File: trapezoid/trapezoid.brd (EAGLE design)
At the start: 90 x 35 mm, 30 parts, among them IC2 LGD20H, U1 MMA8452Q, U2 microSD, U4 MCP73831, Y1 CRYSTAL.ABS25

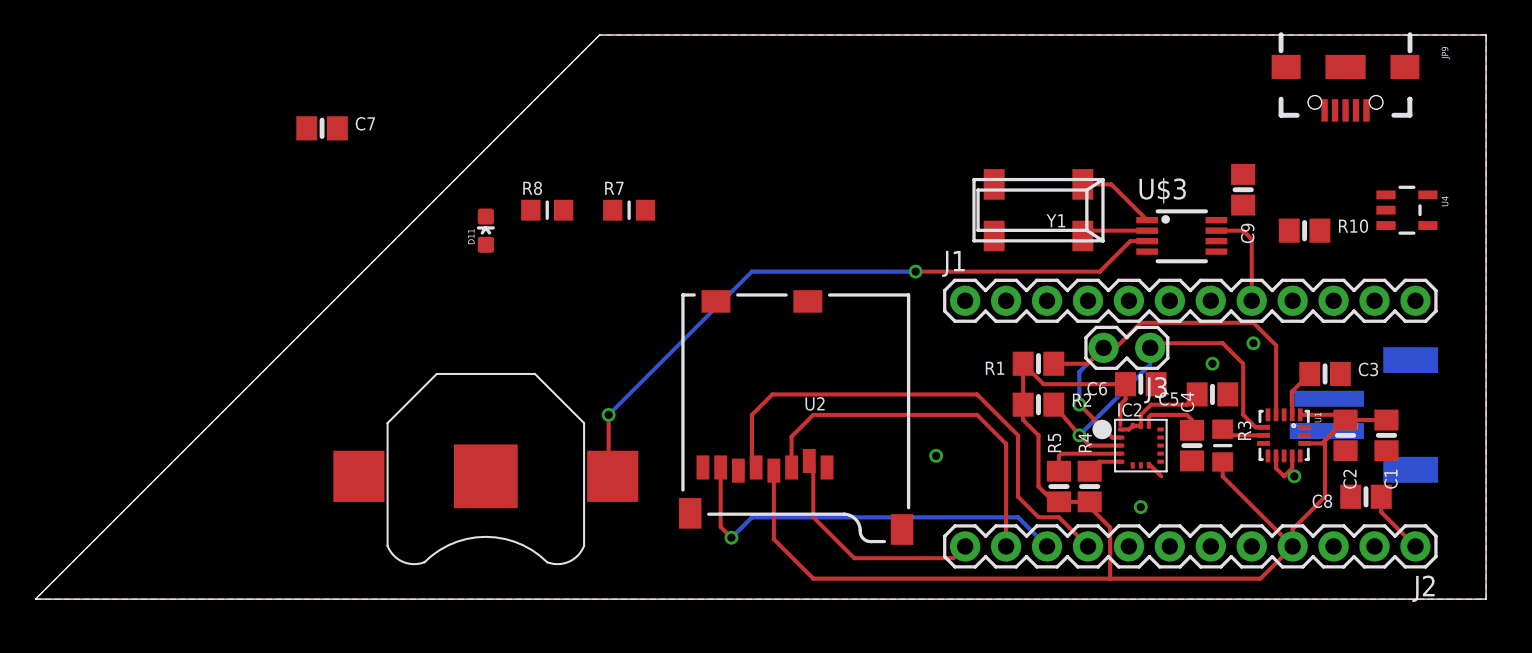
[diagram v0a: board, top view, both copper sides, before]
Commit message: fully connected schematics
had to remove some header pin spots to run wire
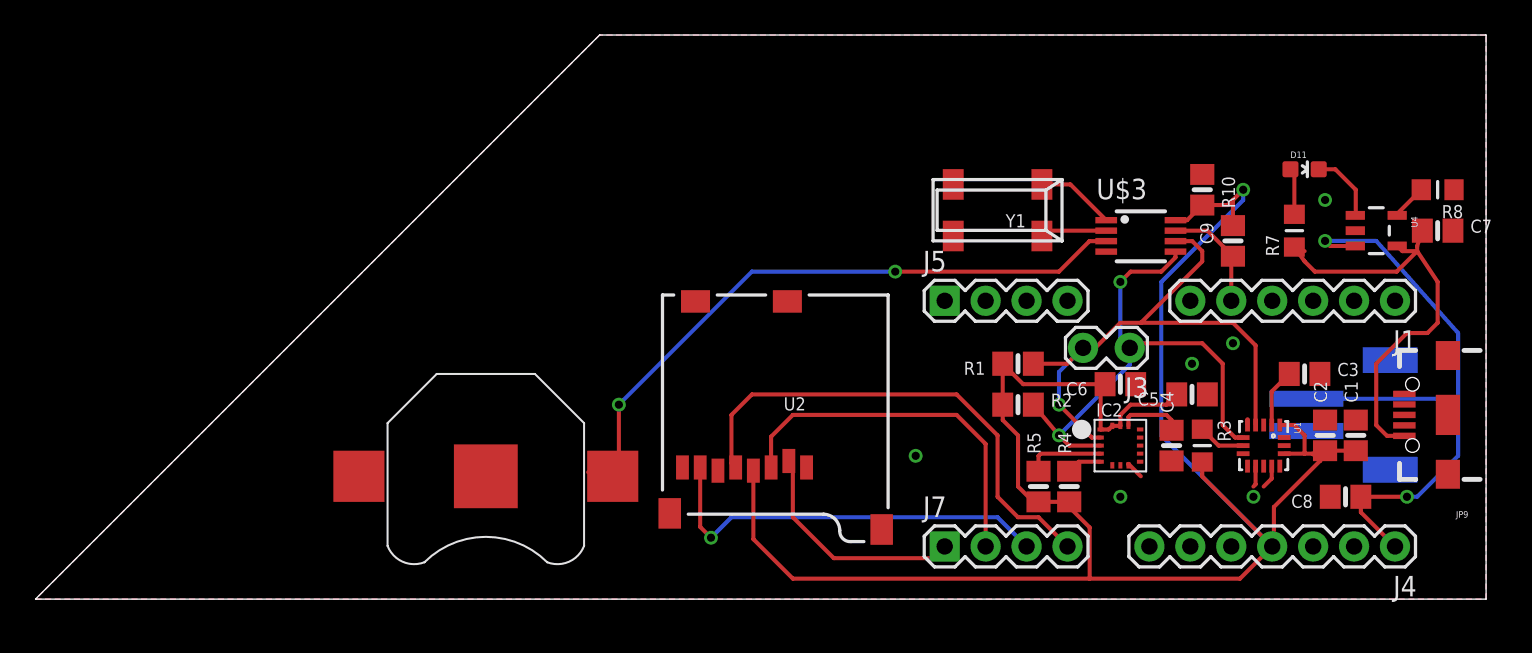
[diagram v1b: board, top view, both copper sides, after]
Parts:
- removed J2: (no value), SparkFun-Connectors:1X12
- added J4: (no value), SparkFun-Connectors:1X07
- added J5, J7: (no value), SparkFun-Connectors:1X04
- J1: device SparkFun-Connectors:1X12 -> SparkFun-Connectors:1X06
- moved C7 69.5 mm to (87.0, 22.9)
- moved R8 55.3 mm to (87.0, 25.4), turned to 180 degrees
- moved D11 50.9 mm to (78.7, 26.7), turned to 270 degrees
- moved R7 41.3 mm to (78.1, 22.9), turned to 90 degrees
- moved J1 26.7 mm to (84.3, 18.5), turned to 180 degrees
- moved JP9 22.5 mm to (87.6, 11.4), turned to 180 degrees
- moved R10 4.49 mm to (74.3, 22.2), turned to 90 degrees
- moved C9 2.54 mm to (72.4, 25.4)
- moved U$3 2.54 mm to (68.6, 22.9)
- moved Y1 2.54 mm to (59.7, 24.1)
- moved U4 2.29 mm to (83.2, 22.9)
- moved C1 1.90 mm to (81.9, 10.2), turned to 90 degrees
- moved U1 1.42 mm to (76.2, 9.53)
- moved C3 1.27 mm to (78.7, 14.0)
- moved C5 1.27 mm to (71.8, 12.7)
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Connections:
- removed net RTC_CS: J1.1
- net +3V3: now also J4.4; no longer J2.4
- net GND: now also J1.4, J4.2; no longer J1.9, J2.2
- net MISO: now also J7.3; no longer J2.10
- net MOSI: now also J7.2; no longer J2.11
- net SCK: now also J7.4; no longer J2.9
- net SD_CS: now also J7.1; no longer J2.12
- net SQW/INT: now also J1.5; no longer J1.8
- net V_RAW: now also J4.1; no longer J2.1
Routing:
- net V_RAW: track 3.96 -> 41.3 mm, vias 0 -> 2
- net +3V3: track 93.8 -> 126.8 mm, vias 0 -> 1
- net VIN: track 0.00 -> 27.8 mm
- net SDA: track 23.7 -> 33.1 mm, vias 1 -> 2
- net SCL: track 27.6 -> 36.2 mm
- net STAT: track 0.00 -> 4.43 mm
- net N$1: track 0.00 -> 2.89 mm
- net PROG: track 0.00 -> 2.21 mm
- net N$4: track 41.8 -> 40.6 mm
- net SA0: track 2.69 -> 3.49 mm
- net SQW/INT: track 6.23 -> 7.03 mm
- net BYP: track 2.99 -> 3.62 mm
- net GND: track 4.40 -> 4.33 mm, vias 5 -> 6

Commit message: decreased board size
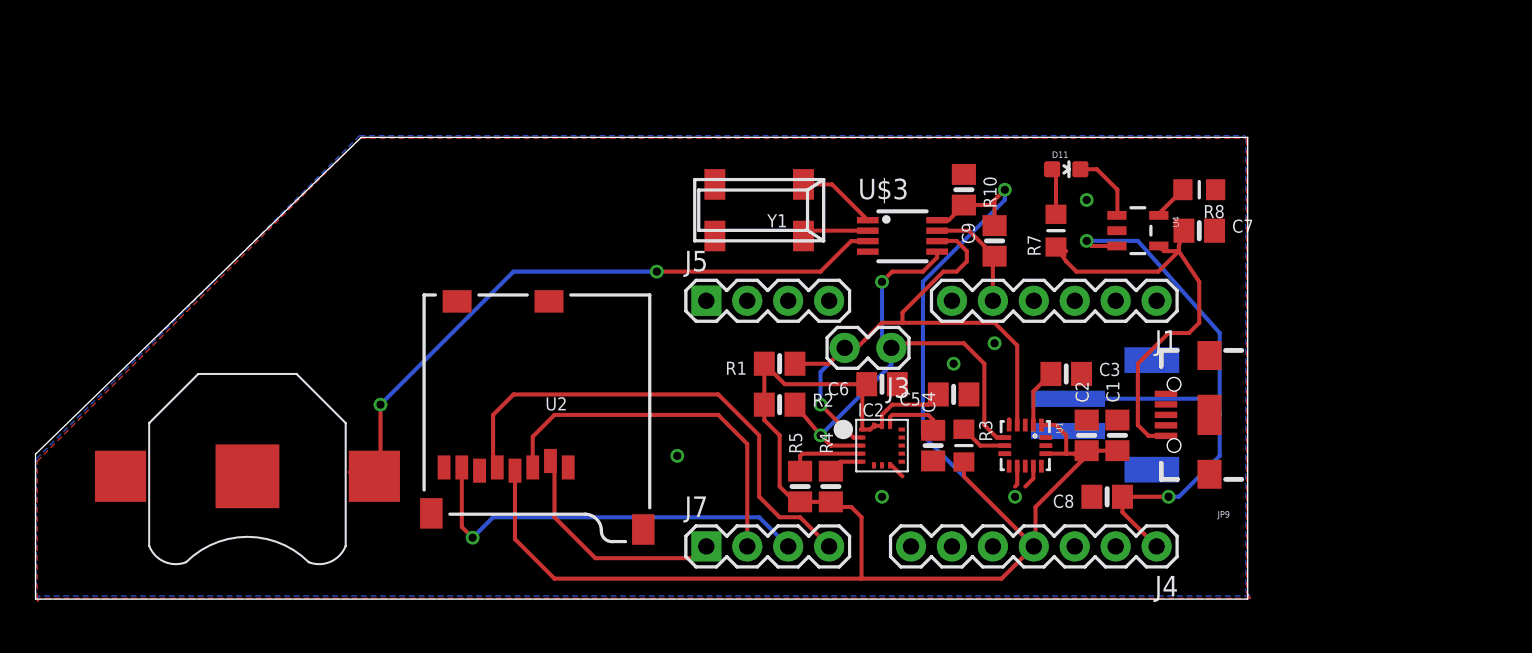
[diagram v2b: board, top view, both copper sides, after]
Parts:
- moved C1 14.8 mm to (67.1, 10.2)
- moved C2 14.8 mm to (65.2, 10.2)
- moved C7 14.8 mm to (72.2, 22.9)
- moved C8 14.8 mm to (66.5, 6.35)
- moved R4 14.8 mm to (49.3, 6.99)
- moved R7 14.8 mm to (63.3, 22.9)
- moved R8 14.8 mm to (72.2, 25.4)
- moved U1 14.8 mm to (61.4, 9.53)
- moved U4 14.8 mm to (68.4, 22.9)
- moved BAT1 14.8 mm to (13.2, 7.62)
- moved C4 14.8 mm to (55.7, 9.53)
- moved C6 14.8 mm to (52.5, 13.3)
- moved C9 14.8 mm to (57.6, 25.4)
- moved IC2 14.8 mm to (52.5, 9.53)
- moved J5 14.8 mm to (41.6, 18.5)
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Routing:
- net +3V3: track 126.8 -> 127.8 mm
- net SCL: track 36.2 -> 37.0 mm
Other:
- board size 90 x 35 mm -> 75.2 x 28.6 mm

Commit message: added gnd vias
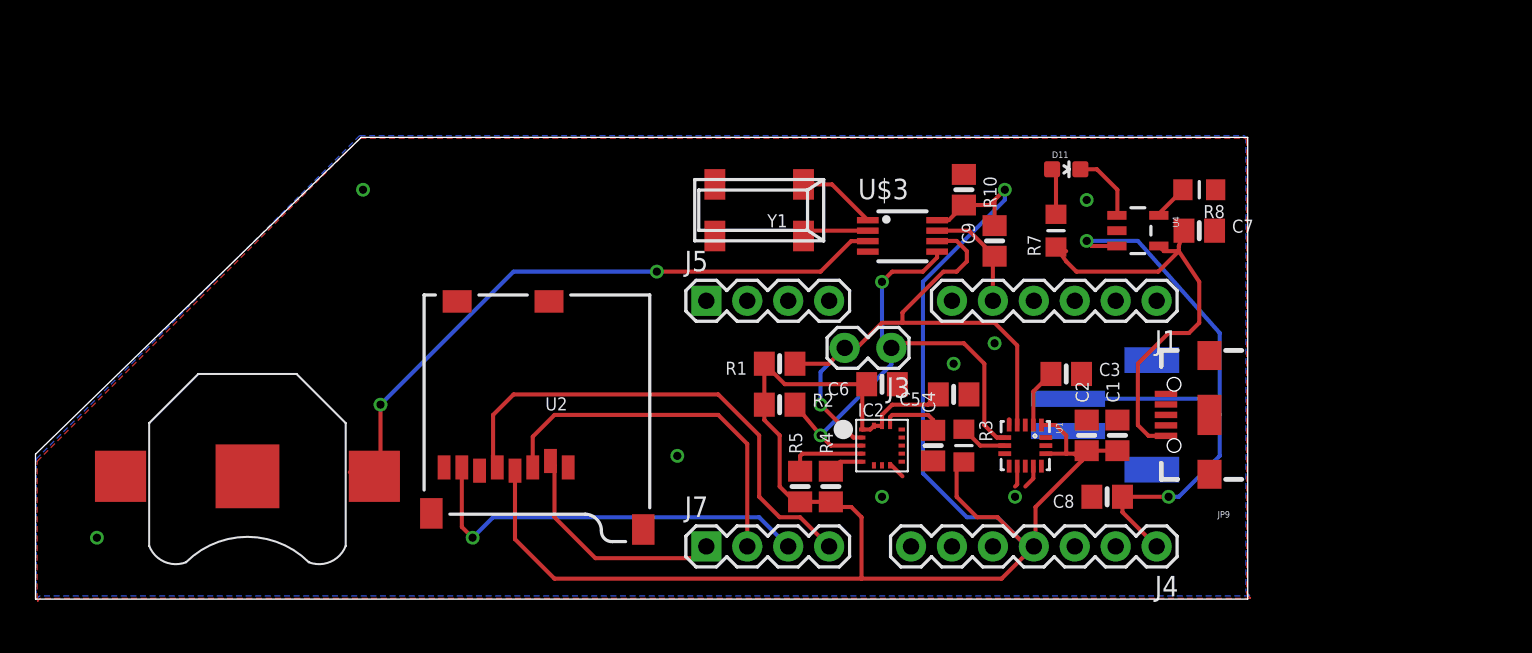
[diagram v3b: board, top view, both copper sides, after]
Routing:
- net +3V3: track 127.8 -> 130.5 mm
- net GND: vias 6 -> 8
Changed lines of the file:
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@@
 <setting verticaltext="up"/>
 </settings>
-<grid distance="0.025" unitdist="inch" unit="inch" style="lines" multiple="1" display="yes" altdistance="0.025" altunitdist="inch" altunit="inch"/>
+<grid distance="0.025" unitdist="inch" unit="inch" style="lines" multiple="1" display="yes" altdistance="0.005" altunitdist="inch" altunit="inch"/>
 <layers>
 <layer number="1" name="Top" color="4" fill="1" visible="yes" active="yes"/>
@@
 <vertex x="0.15" y="-0.15"/>
 </polygon>
+<via x="3.81" y="3.81" extent="1-16" drill="0.508"/>
+<via x="20.32" y="25.4" extent="1-16" drill="0.508"/>
 </signal>
 <signal name="SCL">
@@
 <wire x1="52.52" y1="10.75" x2="52.52" y2="11.43" width="0.254" layer="1"/>
 <wire x1="53.155" y1="12.065" x2="55.38" y2="12.065" width="0.254" layer="1"/>
-<wire x1="57.6" y1="7.61" x2="61.94" y2="3.27" width="0.254" layer="1"/>
 <wire x1="55.38" y1="12.065" x2="56.015" y2="12.7" width="0.254" layer="1"/>
 <wire x1="49.345" y1="6.035" x2="49.345" y2="5.715" width="0.254" layer="1"/>
@@
 <wire x1="45.22" y1="12.065" x2="45.22" y2="14.605" width="0.254" layer="1"/>
 <wire x1="57.6" y1="8.509" x2="57.6" y2="8.255" width="0.254" layer="1"/>
-<wire x1="57.6" y1="7.61" x2="57.6" y2="8.509" width="0.254" layer="1"/>
 <wire x1="67.125" y1="9.21" x2="65.22" y2="9.21" width="0.254" layer="1"/>
 <wire x1="55.94" y1="23.51" x2="56.66" y2="23.51" width="0.254" layer="1"/>
@@
 <wire x1="60.14" y1="25.4" x2="60.14" y2="24.765" width="0.254" layer="16"/>
 <wire x1="60.14" y1="24.765" x2="55.06" y2="19.685" width="0.254" layer="16"/>
-<wire x1="55.06" y1="19.685" x2="55.06" y2="10.15" width="0.254" layer="16"/>
-<wire x1="55.06" y1="10.15" x2="61.94" y2="3.27" width="0.254" layer="16"/>
+<wire x1="55.06" y1="19.685" x2="55.06" y2="7.805" width="0.254" layer="16"/>
 <wire x1="59.505" y1="23.175" x2="59.505" y2="24.765" width="0.254" layer="1"/>
 <wire x1="59.505" y1="24.765" x2="60.14" y2="25.4" width="0.254" layer="1"/>
@@
 <wire x1="50.615" y1="5.715" x2="51.25" y2="5.08" width="0.254" layer="1"/>
 <wire x1="51.25" y1="5.08" x2="51.25" y2="1.27" width="0.254" layer="1"/>
+<wire x1="61.94" y1="3.27" x2="61.5" y2="3.27" width="0.254" layer="1"/>
+<wire x1="61.5" y1="3.27" x2="59.69" y2="5.08" width="0.254" layer="1"/>
+<wire x1="59.69" y1="5.08" x2="58.42" y2="5.08" width="0.254" layer="1"/>
+<wire x1="58.42" y1="5.08" x2="57.15" y2="6.35" width="0.254" layer="1"/>
+<wire x1="57.15" y1="6.35" x2="57.15" y2="8.059" width="0.254" layer="1"/>
+<wire x1="57.15" y1="8.059" x2="57.6" y2="8.509" width="0.254" layer="1"/>
+<wire x1="61.94" y1="3.27" x2="61.5" y2="3.27" width="0.254" layer="16"/>
+<wire x1="61.5" y1="3.27" x2="59.69" y2="5.08" width="0.254" layer="16"/>
+<wire x1="55.06" y1="7.805" x2="57.785" y2="5.08" width="0.254" layer="16"/>
+<wire x1="57.785" y1="5.08" x2="59.69" y2="5.08" width="0.254" layer="16"/>
 </signal>
 <signal name="CS_3.3V">

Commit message: shifted everything so pro mini would not over hang board
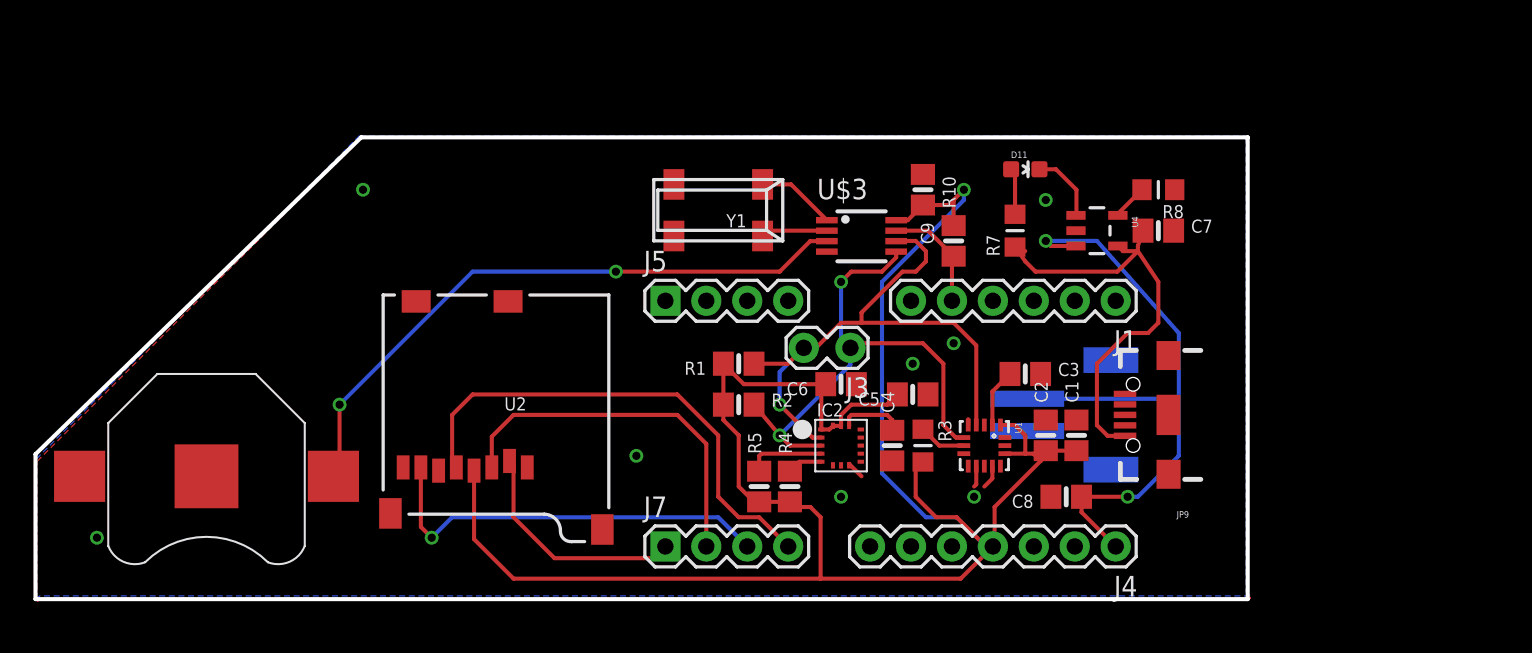
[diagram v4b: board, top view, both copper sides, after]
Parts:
- moved C1 2.54 mm to (64.6, 10.2)
- moved C3 2.54 mm to (61.4, 14.0)
- moved C5 2.54 mm to (54.4, 12.7)
- moved C6 2.54 mm to (50.0, 13.3)
- moved D11 2.54 mm to (61.4, 26.7)
- moved IC2 2.54 mm to (50.0, 9.53)
- moved J1 2.54 mm to (67.0, 18.5)
- moved J4 2.54 mm to (67.0, 3.27)
- moved JP1 2.54 mm to (65.2, 11.4)
- moved JP9 2.54 mm to (70.3, 11.4)
- moved BAT1 2.54 mm to (10.6, 7.62)
- moved C2 2.54 mm to (62.7, 10.2)
- moved C4 2.54 mm to (53.2, 9.53)
- moved C9 2.54 mm to (55.1, 25.4)
- moved J3 2.54 mm to (50.4, 15.6)
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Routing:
- net N$4: track 40.6 -> 39.0 mm
